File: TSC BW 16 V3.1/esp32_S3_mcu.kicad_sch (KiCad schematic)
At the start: 10 parts, among them J3 Free GPIO !pull-up, J4 Free GPIO pull-up, U3 ESP32-S3-WROOM-1

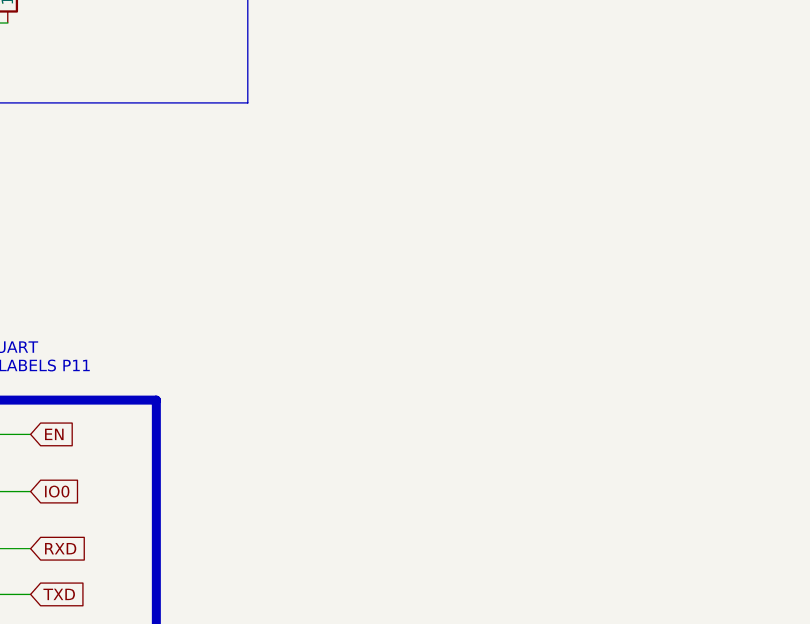
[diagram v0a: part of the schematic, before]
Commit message: TSC V3 added w5500 v3 rework
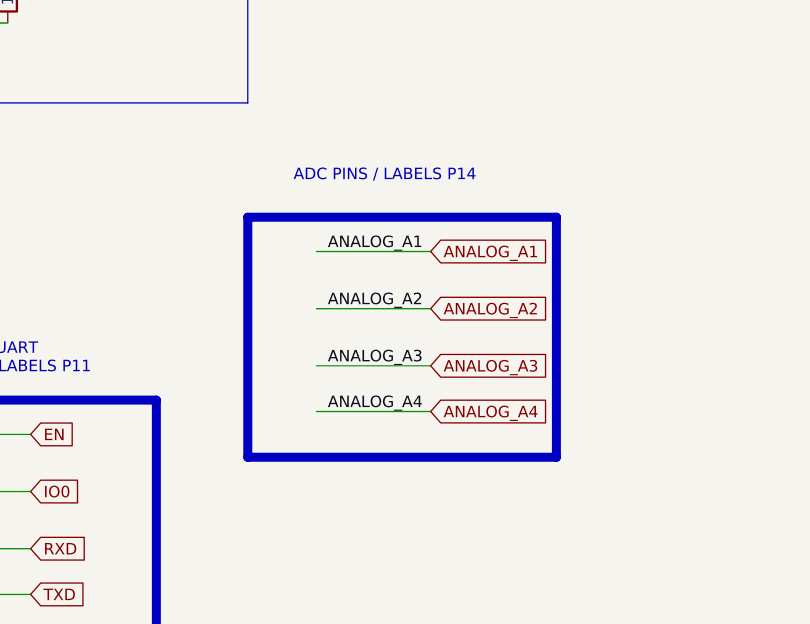
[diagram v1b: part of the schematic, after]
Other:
- note added: "ADC PINS / LABELS P14"
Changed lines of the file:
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@@
+	)
+	(rectangle
+		(start 185.42 137.16)
+		(end 219.71 163.83)
+		(stroke
+			(width 1)
+			(type solid)
+			(color 225 0 0 1)
+		)
+		(fill
+			(type none)
+		)
 	)
 	(rectangle
@@
 		(exclude_from_sim no)
 		(at 156.21 152.908 0)
+		(effects
+			(font
+				(size 1.27 1.27)
+			)
+		)
+	)
+	(text "ADC PINS / LABELS P14"
+		(exclude_from_sim no)
+		(at 200.66 132.588 0)
 		(effects
 			(font
@@
 	(wire
 		(pts
+			(xy 193.04 140.97) (xy 205.74 140.97)
+		)
+		(stroke
+			(width 0)
+			(type default)
+		)
+	)
+	(wire
+		(pts
 			(xy 24.13 160.02) (xy 33.02 160.02)
 		)
@@
 	(wire
 		(pts
+			(xy 193.04 153.67) (xy 205.74 153.67)
+		)
+		(stroke
+			(width 0)
+			(type default)
+		)
+	)
+	(wire
+		(pts
 			(xy 71.12 59.69) (xy 83.82 59.69)
 		)
@@
 	(wire
 		(pts
+			(xy 193.04 147.32) (xy 205.74 147.32)
+		)
+		(stroke
+			(width 0)
+			(type default)
+		)
+	)
+	(wire
+		(pts
 			(xy 71.12 100.33) (xy 83.82 100.33)
 		)
@@
 		(pts
 			(xy 105.41 167.64) (xy 118.11 167.64)
+		)
+		(stroke
+			(width 0)
+			(type default)
+		)
+	)
+	(wire
+		(pts
+			(xy 193.04 158.75) (xy 205.74 158.75)
 		)
 		(stroke
@@
 	)
 	(label "ANALOG_A2"
+		(at 194.31 147.32 0)
+		(effects
+			(font
+				(size 1.27 1.27)
+			)
+			(justify left bottom)
+		)
+	)
+	(label "ANALOG_A2"
 		(at 72.39 74.93 0)
 		(effects
@@
 		)
 	)
+	(label "ANALOG_A3"
+		(at 194.31 153.67 0)
+		(effects
+			(font
+				(size 1.27 1.27)
+			)
+			(justify left bottom)
+		)
+	)
 	(label "ETH_INT"
 		(at 73.66 64.77 0)
@@
 		)
 	)
+	(label "ANALOG_A4"
+		(at 194.31 158.75 0)
+		(effects
+			(font
+				(size 1.27 1.27)
+			)
+			(justify left bottom)
+		)
+	)
 	(label "ANALOG_A3"
 		(at 72.39 77.47 0)
@@
 		)
 	)
+	(label "ANALOG_A1"
+		(at 194.31 140.97 0)
+		(effects
+			(font
+				(size 1.27 1.27)
+			)
+			(justify left bottom)
+		)
+	)
 	(label "485_EN"
 		(at 123.19 69.85 0)
@@
 		)
 	)
+	(global_label "ANALOG_A3"
+		(shape input)
+		(at 205.74 153.67 0)
+		(fields_autoplaced yes)
+		(effects
+			(font
+				(size 1.27 1.27)
+			)
+			(justify left)
+		)
+		(property "Intersheetrefs" "${INTERSHEET_REFS}"
+			(at 219.1272 153.67 0)
+			(hide yes)
+			(show_name no)
+			(do_not_autoplace no)
+			(effects
+				(font
+					(size 1.27 1.27)
+				)
+				(justify left)
+			)
+		)
+	)
+	(global_label "ANALOG_A4"
+		(shape input)
+		(at 205.74 158.75 0)
+		(fields_autoplaced yes)
+		(effects
+			(font
+				(size 1.27 1.27)
+			)
+			(justify left)
+		)
+		(property "Intersheetrefs" "${INTERSHEET_REFS}"
+			(at 219.1272 158.75 0)
+			(hide yes)
+			(show_name no)
+			(do_not_autoplace no)
+			(effects
+				(font
+					(size 1.27 1.27)
+				)
+				(justify left)
+			)
+		)
+	)
 	(global_label "485RX"
 		(shape input)
@@
 			(hide yes)
 			(show_name no)
+			(do_not_autoplace no)
+			(effects
+				(font
+					(size 1.27 1.27)
+				)
+				(justify left)
+			)
+		)
+	)
+	(global_label "ANALOG_A2"
+		(shape input)
+		(at 205.74 147.32 0)
+		(fields_autoplaced yes)
+		(effects
+			(font
+				(size 1.27 1.27)
+			)
+			(justify left)
+		)
+		(property "Intersheetrefs" "${INTERSHEET_REFS}"
+			(at 219.1272 147.32 0)
+			(hide yes)
+			(show_name no)
+			(do_not_autoplace no)
+			(effects
+				(font
+					(size 1.27 1.27)
+				)
+				(justify left)
+			)
+		)
+	)
+	(global_label "ANALOG_A1"
+		(shape input)
+		(at 205.74 140.97 0)
+		(fields_autoplaced yes)
+		(effects
+			(font
+				(size 1.27 1.27)
+			)
+			(justify left)
+		)
+		(property "Intersheetrefs" "${INTERSHEET_REFS}"
+			(at 219.1272 140.97 0)
+			(hide yes)
+			(show_name no)

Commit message: WORKING ON IT
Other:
- note added: "Analog Inputs ANALOG_A1 - PIN4 : GPIO4 ANALOG_A2 - PIN6 : GPIO6 ANALOG_A3 - PIN7 : GPIO7 ANALOG_A4 - PIN5 : GPIO5"
- note added: "BUZZER - PIN25 : GPIO48"
- note added: "Ethernet (W5500) ETH_SCLK - PIN35 : GPIO42 ETH_MOSI - PIN37 : GPIO43 ETH_MISO - PIN36 : GPIO44 ETH_SCS - PIN8 : GPIO15 ETH_INT - PIN38 : GPIO2 ETH_RST - PIN39 : GPIO1"
- note added: "FREE GPIO with pull-up on PCB 1 - PIN31 : GPIO38 2 - PIN24 : GPIO47 3 - PIN25 : GPIO48"
- note added: "Free GPIOs (without pull-up on PCB) 1 - PIN32 : GPIO39 2 - PIN33 : GPIO40 3 - PIN34 : GPIO41"
- note added: "RS485 TXD - PIN9 : GPIO16 RXD - PIN10 : GPIO17 TXD - PIN23 : GPIO21"
- note added: "SD Card (SPI) MOSI - PIN20 : GPIO12 SCK - PIN21 : GPIO13 MISO - PIN22 : GPIO14 CS - PIN19 : GPIO11 SD-CD - PIN23 : GPIO21"
- note added: "SDA - PIN17 : GPIO9 SCL - PIN18 : GPIO10"
- note added: "USB C - UART EN- PIN3 : NO GPIO IO0 - PIN27 : GPIO0 RXD - PIN36/RXD0 : GPIO44,U0RXD TXD - PIN37/ TXD0 : GPIO43,U0TXD"
- moved on the sheet: J3

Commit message: WORKING ON IT
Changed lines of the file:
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@@
 	(text "SDA - PIN17 : GPIO9\nSCL - PIN18 : GPIO10"
 		(exclude_from_sim no)
-		(at 34.544 187.706 0)
+		(at 23.622 189.738 0)
 		(effects
 			(font
@@
 				(color 33 191 7 1)
 			)
+			(justify left)
 		)
 	)
